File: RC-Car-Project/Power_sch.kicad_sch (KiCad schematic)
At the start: 20 parts, among them U2 A6986F3V3TR

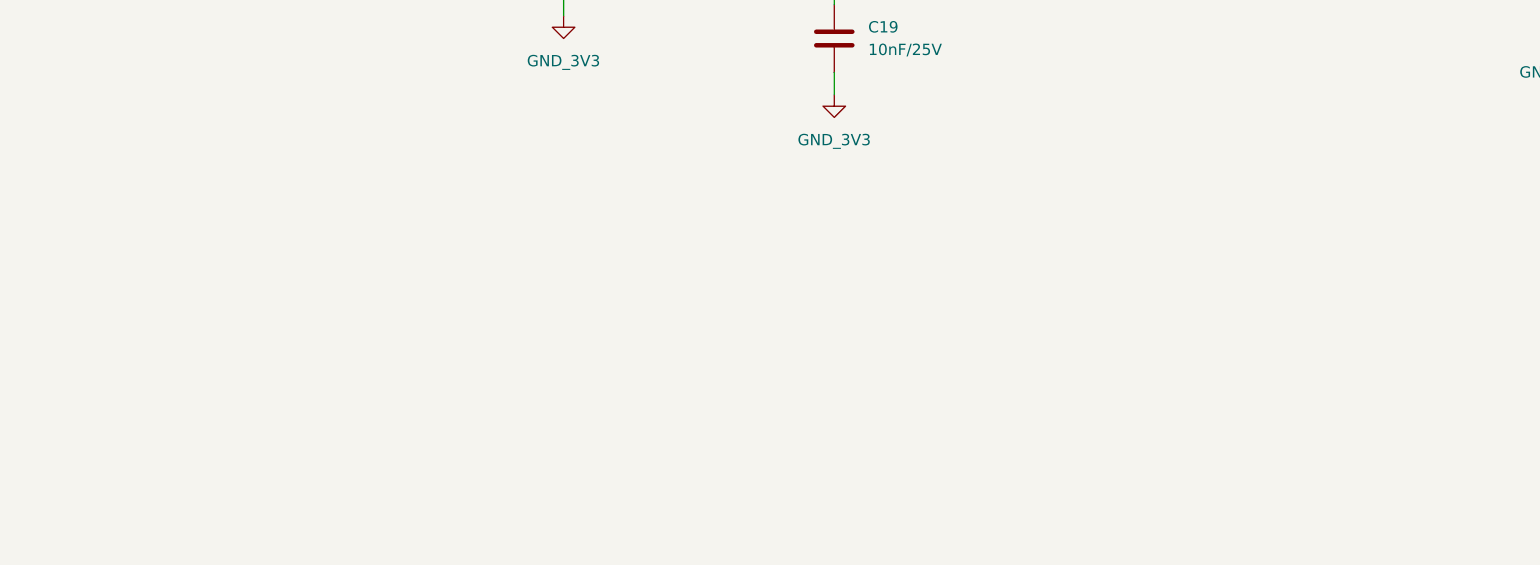
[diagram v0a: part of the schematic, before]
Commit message: Readd 12V buck
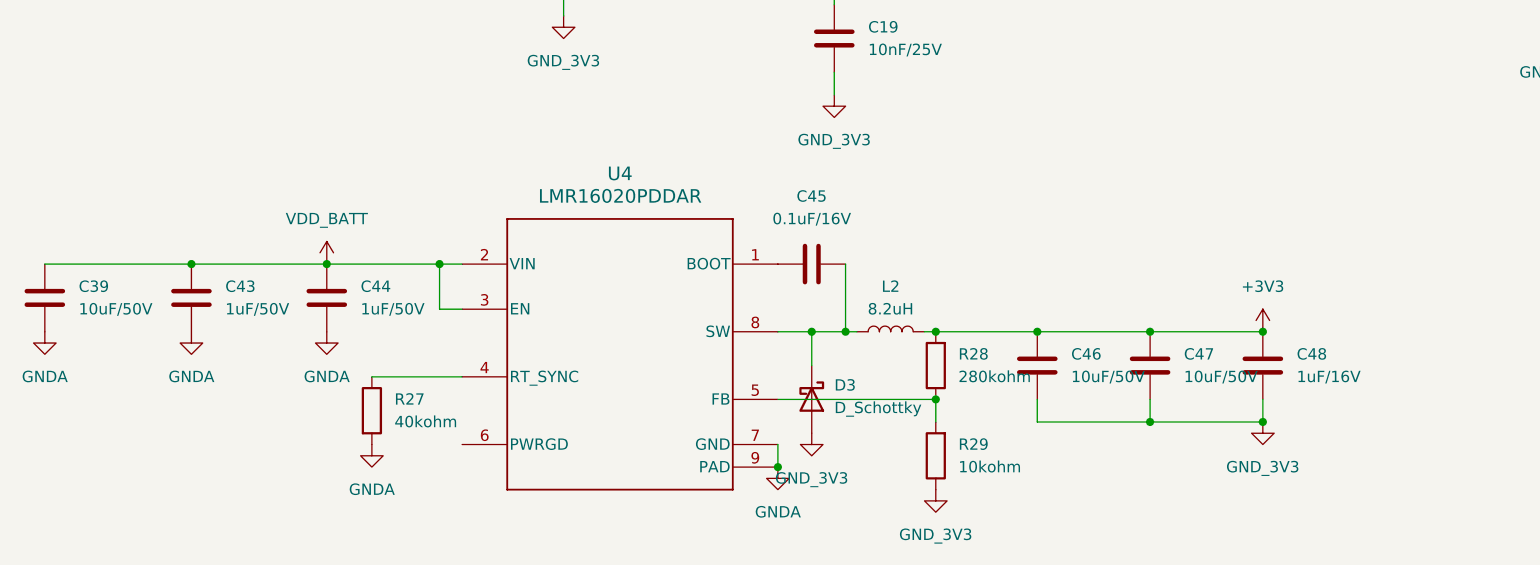
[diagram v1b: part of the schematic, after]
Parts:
- added C39, C46, C47: 10uF/50V, Capacitor_SMD:C_1210_3225Metric, symbol Device:C
- added C43, C44: 1uF/50V, Capacitor_SMD:C_0201_0603Metric, symbol Device:C
- added C45: 0.1uF/16V, Capacitor_SMD:C_0201_0603Metric, symbol Device:C
- added C48: 1uF/16V, Capacitor_SMD:C_0201_0603Metric, symbol Device:C
- added D3: D_Schottky, Diode_SMD:Nexperia_CFP3_SOD-123W, symbol Device:D_Schottky
- added L2: 8.2uH, Inductor_SMD:L_Wuerth_MAPI-4030, symbol Device:L
- added R27: 40kohm, Resistor_SMD:R_0201_0603Metric, symbol Device:R
- added R28: 280kohm, Resistor_SMD:R_0201_0603Metric, symbol Device:R
- added R29: 10kohm, Resistor_SMD:R_0201_0603Metric, symbol Device:R
- added U4: LMR16020PDDAR, footprints:DDA0008E_N, symbol LMR16020PDDAR:LMR16020PDDAR
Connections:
- net +3V3: now also C46.1, C47.1, C48.1, L2.2, R28.2
- net GNDA: now also C39.2, C43.2, C44.2, R27.2, U4.7 (GND), U4.9 (PAD)
- net GND_3V3: now also C46.2, C47.2, C48.2, D3.2 (A), R29.1
- net VDD_BATT: now also C39.1, C43.1, C44.1, U4.2 (VIN), U4.3 (EN)
- new net: C45.1, D3.1 (K), L2.1, U4.8 (SW)
- new net: C45.2, U4.1 (BOOT)
- new net: R28.1, R29.2, U4.5 (FB)
- new net: R27.1, U4.4 (RT_SYNC)

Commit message: Fix power
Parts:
- R10: value 100kohm -> 10kohm
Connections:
- net +3V3: no longer C46.1, C47.1, C48.1, L2.2, R28.2
- new net +12V: C46.1, C47.1, C48.1, L2.2, R28.2
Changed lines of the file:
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@@
 	(paper "A4")
 	(junction
+		(at 161.29 163.83)
+		(diameter 0)
+		(color 0 0 0 0)
+	)
+	(junction
 		(at 194.31 120.65)
 		(diameter 0)
@@
 	)
 	(junction
-		(at 161.29 163.83)
-		(diameter 0)
-		(color 0 0 0 0)
-	)
-	(junction
 		(at 185.42 120.65)
 		(diameter 0)
@@
 	(symbol
 		(lib_id "power:+3V3")
-		(at 161.29 163.83 0)
-		(unit 1)
-		(exclude_from_sim no)
-		(in_bom yes)
-		(on_board yes)
-		(dnp no)
-		(fields_autoplaced yes)
-		(property "Reference" "#PWR0119"
-			(at 161.29 167.64 0)
-			(effects
-				(font
-					(size 1.27 1.27)
-				)
-				(hide yes)
-			)
-		)
-		(property "Value" "+3V3"
-			(at 161.29 158.75 0)
-			(effects
-				(font
-					(size 1.27 1.27)
-				)
-			)
-		)
-		(property "Footprint" ""
-			(at 161.29 163.83 0)
-			(effects
-				(font
-					(size 1.27 1.27)
-				)
-				(hide yes)
-			)
-		)
-		(property "Datasheet" ""
-			(at 161.29 163.83 0)
-			(effects
-				(font
-					(size 1.27 1.27)
-				)
-				(hide yes)
-			)
-		)
-		(property "Description" "Power symbol creates a global label with name \"+3V3\""
-			(at 161.29 163.83 0)
-			(effects
-				(font
-					(size 1.27 1.27)
-				)
-				(hide yes)
-			)
-		)
-		(pin "1"
-		)
-		(instances
-			(project "RC-Car-Project"
-				(path "/ba870fd1-751d-4755-8e1a-1ea86ca9e2f6/e8cbdd69-5fc8-4583-a262-8a3c06e86dab"
-					(reference "#PWR0119")
-					(unit 1)
-				)
-			)
-		)
-	)
-	(symbol
-		(lib_id "power:+3V3")
 		(at 227.33 107.95 0)
 		(unit 1)
@@
 			)
 		)
-		(property "Value" "100kohm"
+		(property "Value" "10kohm"
 			(at 196.85 126.9999 0)
 			(effects
@@
 					(unit 1)
 				)
+			)
+		)
+	)
+	(symbol
+		(lib_id "power:+3V3")
+		(at 161.29 163.83 0)
+		(unit 1)
+		(exclude_from_sim no)
+		(in_bom yes)
+		(on_board yes)
+		(dnp no)
+		(fields_autoplaced yes)
+		(property "Reference" "#PWR0122"
+			(at 161.29 167.64 0)
+			(effects
+				(font
+					(size 1.27 1.27)
+				)
+				(hide yes)
+			)
+		)
+		(property "Value" "+12V"
+			(at 161.29 158.75 0)
+			(effects
+				(font
+					(size 1.27 1.27)
+				)
+			)
+		)
+		(property "Footprint" ""
+			(at 161.29 163.83 0)
+			(effects
+				(font
+					(size 1.27 1.27)
+				)
+				(hide yes)
+			)
+		)
+		(property "Datasheet" ""
+			(at 161.29 163.83 0)
+			(effects
+				(font
+					(size 1.27 1.27)
+				)
+				(hide yes)
+			)
+		)
+		(property "Description" "Power symbol creates a global label with name \"+3V3\""
+			(at 161.29 163.83 0)
+			(effects
+				(font
+					(size 1.27 1.27)
+				)
+				(hide yes)
+			)
+		)
+		(pin "1"
+		)
+		(instances
+			(project "RC-Car-Project"
+				(path "/ba870fd1-751d-4755-8e1a-1ea86ca9e2f6/e8cbdd69-5fc8-4583-a262-8a3c06e86dab"
+					(reference "#PWR0122")
+					(unit 1)
+				)

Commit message: Fixed Annotations
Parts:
- C1: renamed from C39; footprint Capacitor_SMD:C_1210_3225Metric -> Capacitor_SMD:C_0603_1608Metric
- C10: renamed from C46; footprint Capacitor_SMD:C_1210_3225Metric -> Capacitor_SMD:C_0603_1608Metric
- C11: renamed from C47; footprint Capacitor_SMD:C_1210_3225Metric -> Capacitor_SMD:C_0603_1608Metric
- C12: renamed from C48; footprint Capacitor_SMD:C_0201_0603Metric -> Capacitor_SMD:C_0603_1608Metric
- C13: renamed from C23; footprint Capacitor_SMD:C_0201_0603Metric -> Capacitor_SMD:C_0603_1608Metric
- C14: renamed from C15; footprint Capacitor_SMD:C_1210_3225Metric -> Capacitor_SMD:C_0603_1608Metric
- C15: renamed from C2; footprint Capacitor_SMD:C_1210_3225Metric -> Capacitor_SMD:C_0603_1608Metric
- C16: footprint Capacitor_SMD:C_0201_0603Metric -> Capacitor_SMD:C_0603_1608Metric
- C17: renamed from C14; footprint Capacitor_SMD:C_1210_3225Metric -> Capacitor_SMD:C_0603_1608Metric
- C18: renamed from C1; footprint Capacitor_SMD:C_0201_0603Metric -> Capacitor_SMD:C_0603_1608Metric
- C19: renamed from C22; footprint Capacitor_SMD:C_0201_0603Metric -> Capacitor_SMD:C_0603_1608Metric
- C2: renamed from C43; footprint Capacitor_SMD:C_0201_0603Metric -> Capacitor_SMD:C_0603_1608Metric
- C3: renamed from C44; footprint Capacitor_SMD:C_0201_0603Metric -> Capacitor_SMD:C_0603_1608Metric
- C4: renamed from C17; footprint Capacitor_SMD:C_0201_0603Metric -> Capacitor_SMD:C_0603_1608Metric
- C5: renamed from C18; footprint Capacitor_SMD:C_0201_0603Metric -> Capacitor_SMD:C_0603_1608Metric
- C6: renamed from C20; footprint Capacitor_SMD:C_0201_0603Metric -> Capacitor_SMD:C_0603_1608Metric
- C7: renamed from C37; footprint Capacitor_SMD:C_0201_0603Metric -> Capacitor_SMD:C_0603_1608Metric
- C8: renamed from C45; footprint Capacitor_SMD:C_0201_0603Metric -> Capacitor_SMD:C_0603_1608Metric
- C9: renamed from C19; footprint Capacitor_SMD:C_0201_0603Metric -> Capacitor_SMD:C_0603_1608Metric
- R10: renamed from R29; footprint Resistor_SMD:R_0201_0603Metric -> Resistor_SMD:R_0603_1608Metric
- R11: renamed from R8; footprint Resistor_SMD:R_0201_0603Metric -> Resistor_SMD:R_0603_1608Metric
- R12: renamed from R9; footprint Resistor_SMD:R_0201_0603Metric -> Resistor_SMD:R_0603_1608Metric
- R13: renamed from R10; footprint Resistor_SMD:R_0201_0603Metric -> Resistor_SMD:R_0603_1608Metric
- R5: renamed from R27; footprint Resistor_SMD:R_0201_0603Metric -> Resistor_SMD:R_0603_1608Metric
- R6: renamed from R21; footprint Resistor_SMD:R_0201_0603Metric -> Resistor_SMD:R_0603_1608Metric
- R7: footprint Resistor_SMD:R_0201_0603Metric -> Resistor_SMD:R_0603_1608Metric
- R8: renamed from R22; footprint Resistor_SMD:R_0201_0603Metric -> Resistor_SMD:R_0603_1608Metric
- R9: renamed from R28; footprint Resistor_SMD:R_0201_0603Metric -> Resistor_SMD:R_0603_1608Metric
- renumbered L2 to L1, L1 to L2, U4 to U1
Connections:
- no-connect marks 1 -> 2

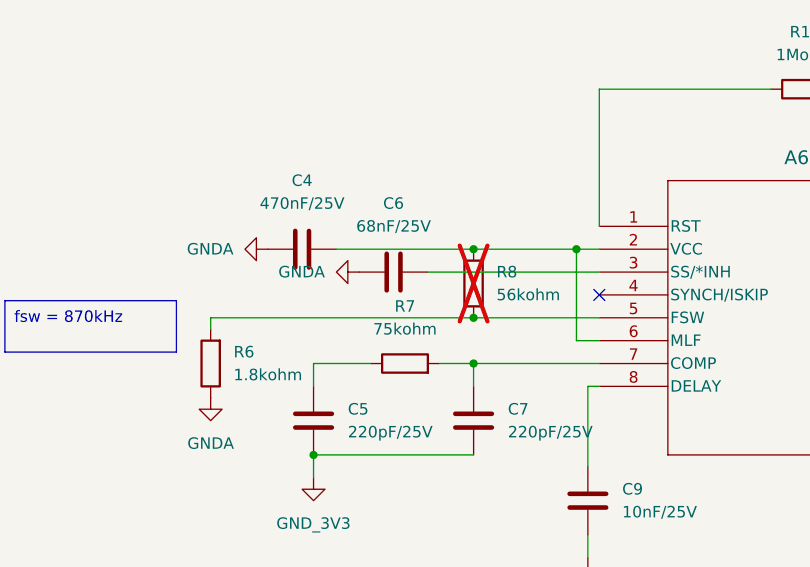
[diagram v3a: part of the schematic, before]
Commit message: Add RF filter + another thermo header + layout everything
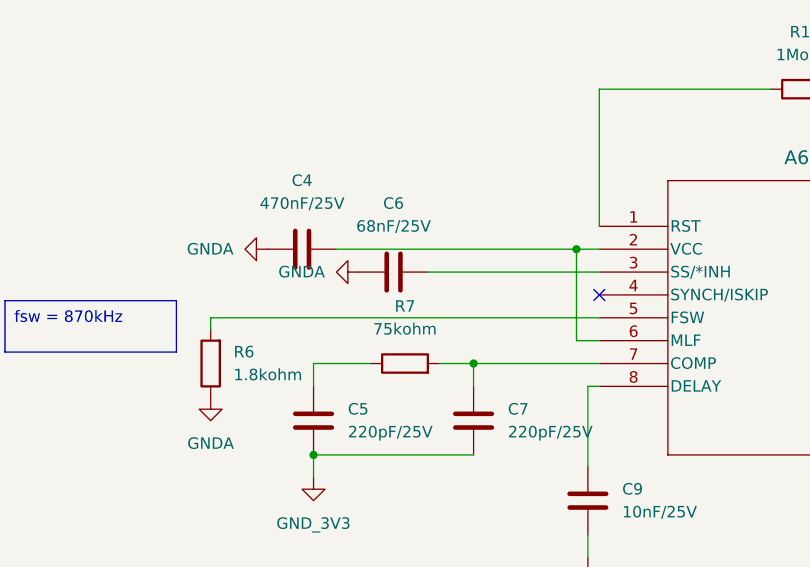
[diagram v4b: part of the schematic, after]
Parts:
- removed R8: 56kohm, Resistor_SMD:R_0603_1608Metric, symbol Device:R
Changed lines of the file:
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@@
 	)
 	(junction
-		(at 100.33 102.87)
-		(diameter 0)
-		(color 0 0 0 0)
-	)
-	(junction
 		(at 124.46 163.83)
 		(diameter 0)
@@
 	)
 	(junction
-		(at 100.33 110.49)
-		(diameter 0)
-		(color 0 0 0 0)
-	)
-	(junction
 		(at 148.59 163.83)
 		(diameter 0)
@@
 	(wire
 		(pts
-			(xy 100.33 110.49) (xy 114.3 110.49)
+			(xy 71.12 110.49) (xy 114.3 110.49)
 		)
 		(stroke
@@
 	(wire
 		(pts
-			(xy 85.09 102.87) (xy 100.33 102.87)
-		)
-		(stroke
-			(width 0)
-			(type default)
-		)
-	)
-	(wire
-		(pts
 			(xy 60.96 168.91) (xy 71.12 168.91)
 		)
@@
 	(wire
 		(pts
-			(xy 71.12 110.49) (xy 100.33 110.49)
-		)
-		(stroke
-			(width 0)
-			(type default)
-		)
-	)
-	(wire
-		(pts
 			(xy 40.64 156.21) (xy 55.88 156.21)
 		)
@@
 	(wire
 		(pts
-			(xy 100.33 102.87) (xy 111.76 102.87)
+			(xy 85.09 102.87) (xy 111.76 102.87)
 		)
 		(stroke
@@
 					(unit 1)
 				)
-			)
-		)
-	)
-	(symbol
-		(lib_id "Device:R")
-		(at 100.33 106.68 180)
-		(unit 1)
-		(exclude_from_sim no)
-		(in_bom yes)
-		(on_board yes)
-		(dnp yes)
-		(fields_autoplaced yes)
-		(property "Reference" "R8"
-			(at 102.87 105.4099 0)
-			(effects
-				(font
-					(size 1.27 1.27)
-				)
-				(justify right)
-			)
-		)
-		(property "Value" "56kohm"
-			(at 102.87 107.9499 0)
-			(effects
-				(font
-					(size 1.27 1.27)
-				)
-				(justify right)
-			)
-		)
-		(property "Footprint" "Resistor_SMD:R_0603_1608Metric"
-			(at 102.108 106.68 90)
-			(effects
-				(font
-					(size 1.27 1.27)
-				)
-				(hide yes)
-			)
-		)
-		(property "Datasheet" "~"
-			(at 100.33 106.68 0)
-			(effects
-				(font
-					(size 1.27 1.27)
-				)
-				(hide yes)
-			)
-		)
-		(property "Description" "Resistor"
-			(at 100.33 106.68 0)
-			(effects
-				(font
-					(size 1.27 1.27)
-				)
-				(hide yes)
-			)
-		)
-		(pin "2"
-		)
-		(pin "1"
-		)
-		(instances
-			(project "RC-Car-Project"
-				(path "/ba870fd1-751d-4755-8e1a-1ea86ca9e2f6/e8cbdd69-5fc8-4583-a262-8a3c06e86dab"
-					(reference "R8")
-					(unit 1)
-				)

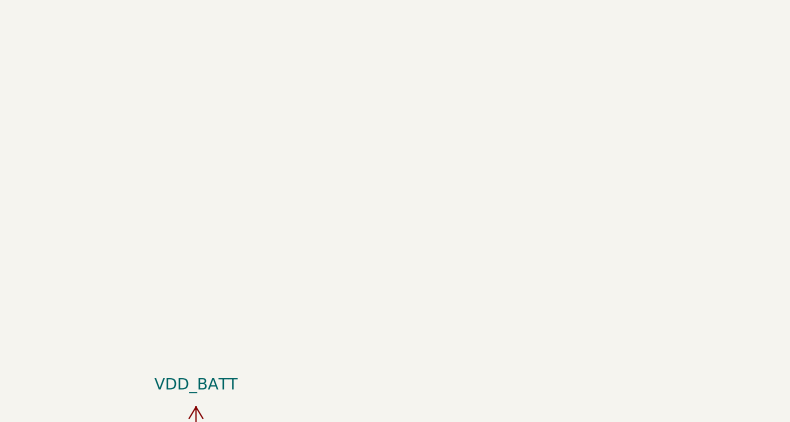
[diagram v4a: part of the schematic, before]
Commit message: Add switch
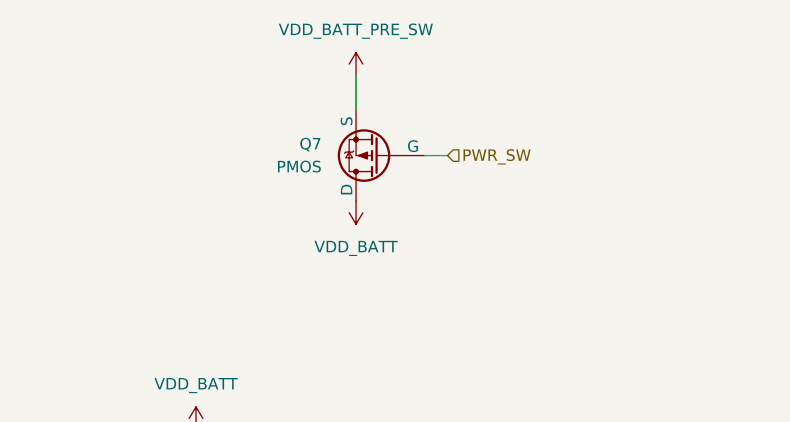
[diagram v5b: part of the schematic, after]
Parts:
- added Q7: PMOS, Package_TO_SOT_SMD:TO-263-2, symbol Simulation_SPICE:PMOS
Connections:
- net VDD_BATT: now also Q7.1 (D)
- new net PWR_SW: Q7.2 (G)
- new net VDD_BATT_PRE_SW: Q7.3 (S)

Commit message: Add Bulk dcaps, layout HV sw, change mosfet footprint to TH
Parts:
- Q7: footprint Package_TO_SOT_SMD:TO-263-2 -> Package_TO_SOT_THT:TO-220-3_Horizontal_TabDown
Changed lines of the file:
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@@
 			)
 		)
-		(property "Footprint" "Package_TO_SOT_SMD:TO-263-2"
+		(property "Footprint" "Package_TO_SOT_THT:TO-220-3_Horizontal_TabDown"
 			(at 191.77 49.53 0)
 			(effects
